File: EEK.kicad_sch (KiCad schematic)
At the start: 50 parts, among them J1 Screw_Terminal_01x02

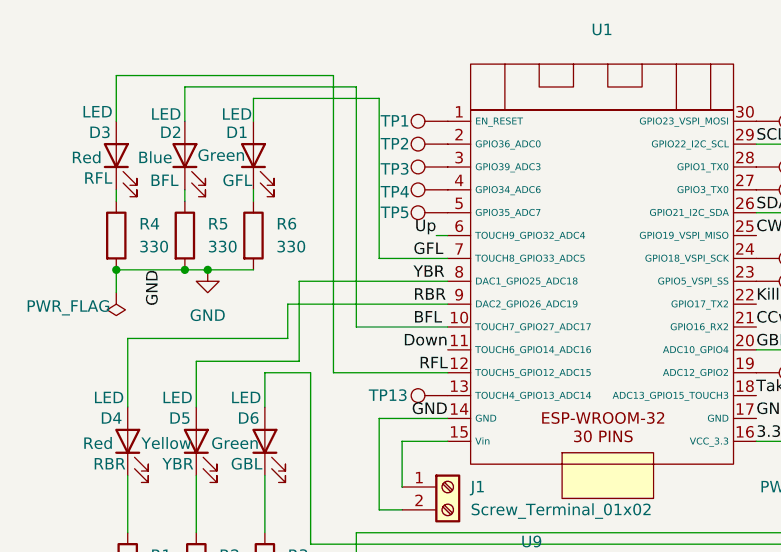
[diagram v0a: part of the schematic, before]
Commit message: change yellow led connection from GPIO 25 to GPIO 35
Change the connection of tellow led that is has an issue when the wifi is used
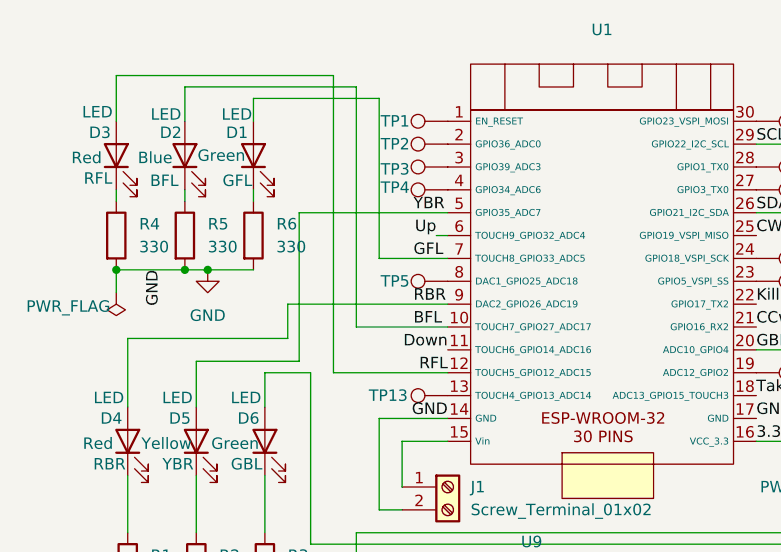
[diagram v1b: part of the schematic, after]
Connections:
- net YBR: now also U1.5 (GPIO35_ADC7); no longer U1.8 (DAC1_GPIO25_ADC18)
- net at TP5.1: now also U1.8 (DAC1_GPIO25_ADC18); no longer U1.5 (GPIO35_ADC7)
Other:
- moved on the sheet: TP5
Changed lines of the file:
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@@
+	(wire
+		(pts
+			(xy 62.23 58.42) (xy 78.74 58.42)
+		)
+		(stroke
+			(width 0)
+			(type default)
+		)
+	)
 	(wire
 		(pts
@@
 	(wire
 		(pts
-			(xy 62.23 66.04) (xy 78.74 66.04)
-		)
-		(stroke
-			(width 0)
-			(type default)
-		)
-	)
-	(wire
-		(pts
 			(xy 113.03 73.66) (xy 124.46 73.66)
 		)
@@
 	(wire
 		(pts
+			(xy 62.23 58.42) (xy 62.23 74.93)
+		)
+		(stroke
+			(width 0)
+			(type default)
+		)
+	)
+	(wire
+		(pts
 			(xy 207.01 107.95) (xy 217.17 107.95)
 		)
@@
 		(pts
 			(xy 43.18 105.41) (xy 50.8 105.41)
-		)
-		(stroke
-			(width 0)
-			(type default)
-		)
-	)
-	(wire
-		(pts
-			(xy 62.23 66.04) (xy 62.23 74.93)
 		)
 		(stroke
@@
 	)
 	(label "YBR"
-		(at 74.93 66.04 0)
+		(at 74.93 58.42 0)
 		(fields_autoplaced yes)
 		(effects
@@
 	(symbol
 		(lib_id "Connector:TestPoint")
-		(at 78.74 58.42 90)
+		(at 78.74 66.04 90)
 		(unit 1)
 		(exclude_from_sim no)
@@
 		(dnp no)
 		(property "Reference" "TP5"
-			(at 72.898 58.42 90)
+			(at 72.898 66.04 90)
 			(effects
 				(font
@@
 		)
 		(property "Value" "TestPoint"
-			(at 69.85 54.356 90)
+			(at 69.85 61.976 90)
 			(effects
 				(font
@@
 		)
 		(property "Footprint" "TestPoint:TestPoint_Plated_Hole_D2.0mm"
-			(at 78.74 53.34 0)
+			(at 78.74 60.96 0)
 			(effects
 				(font
@@
 		)
 		(property "Datasheet" "~"
-			(at 78.74 53.34 0)
+			(at 78.74 60.96 0)
 			(effects
 				(font
@@
 		)
 		(property "Description" "test point"
-			(at 78.74 58.42 0)
+			(at 78.74 66.04 0)
 			(effects
 				(font
@@
 		(dnp no)
 		(property "Reference" "TP4"
-			(at 72.898 56.134 90)
-			(effects
-				(font
+			(at 72.898 55.626 90)
+			(effects
+				(font
